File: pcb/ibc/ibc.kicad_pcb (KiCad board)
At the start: 2 copper layers, 87 x 80 mm, 72 parts, among them J1 MOLEX_0039291067, J2 CONN_01X03, J3 CONN_01X05, J4 MOLEX_0532610571, J5 U.FL, J6 U.FL, J7 U.FL, J8 U.FL, J9 MOLEX_0039291087, M1 LOGO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

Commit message: Finished v0.1 IBC ready for fab
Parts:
- added J10: GROUND, azonenberg_pcb:TESTPOINT_SMT_KEYSTONE_5016, F.Cu at (35.3, 52.7)
- added J11: GROUND, azonenberg_pcb:TESTPOINT_SMT_KEYSTONE_5016, F.Cu at (96.2, 78.5)
- moved C6 52.8 mm to (78.6, 79.7), turned to 180 degrees
- moved C4 52.5 mm to (78.0, 76.6), turned to 180 degrees
- moved C5 47.9 mm to (85.9, 86.0), turned to 180 degrees
- moved C9 46.7 mm to (86.6, 83.3)
- moved C8 40.8 mm to (86.7, 81.3)
- moved R9 38.3 mm to (99.4, 96.7), turned to 180 degrees
- moved R5 35.7 mm to (83.8, 85.5), turned to -90 degrees
- moved C3 33.6 mm to (92.2, 85.0), turned to -90 degrees
- moved FB2 29.5 mm to (91.5, 83.5)
- moved R23 1.16 mm to (95.8, 59.5), turned to -90 degrees
- moved R19 1.00 mm to (75.2, 82.8)
- moved R6 1.00 mm to (75.2, 81.2)
- moved R1 0.50 mm to (99.4, 69.5)
- moved R13 0.50 mm to (74.5, 59.5)
- moved R2 0.50 mm to (99.4, 71.5)
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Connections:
- U1 pad 10: /12V0_VSENSE -> /12V0_OUT_EN
- U1 pad 11: /12V0_OK -> /TEMP_ALERT
- U1 pad 12: unconnected-(U1-Pad12) -> /12V0_OK
- U1 pad 13: /LOAD_PGOOD -> /12V_SHUNT_VOUT
- U1 pad 14: /12V0_OUT_EN -> /12V0_REMOTE_VSENSE
- U1 pad 15: /12V0_REMOTE_VSENSE -> /12V0_VSENSE
- U1 pad 6: /TEMP_ALERT -> unconnected-(U1-Pad6)
- U1 pad 7: /12V_SHUNT_VOUT -> /48V_SHUNT_VOUT
- U1 pad 8: /48V_SHUNT_VOUT -> /48V0_VSENSE
- U1 pad 9: /48V0_VSENSE -> /LOAD_PGOOD
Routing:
- net /GND: track 0.00 -> 478.2 mm, vias 0 -> 151
- net /3V3_SB: track 0.00 -> 224.4 mm, vias 0 -> 9
- net /12V0_OUT_EN: track 0.00 -> 124.8 mm, vias 0 -> 3
- net /LOAD_PGOOD: track 0.00 -> 119.9 mm, vias 0 -> 2
- net /I2C_SDA: track 0.00 -> 82.6 mm, vias 0 -> 4
- net /I2C_SCL: track 0.00 -> 81.4 mm, vias 0 -> 2
- net /12V0_VSENSE: track 0.00 -> 77.7 mm
- net /12V_SHUNT_VOUT: track 0.00 -> 56.9 mm, vias 0 -> 2
- net /TEMP_ALERT: track 0.00 -> 54.6 mm, vias 0 -> 2
- net /12V0: track 0.00 -> 51.2 mm
- net /GND_RAW: track 0.00 -> 48.7 mm
- net /12V0_SENSE: track 0.00 -> 40.0 mm, vias 0 -> 2
- net /12V0_OK: track 0.00 -> 35.8 mm, vias 0 -> 2
- net /12V0_SWIN: track 0.00 -> 35.1 mm, vias 0 -> 6
- net /48V_SHIN: track 0.00 -> 31.7 mm
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- added copper zone on F.Cu, net /12V0
- added copper zone on F.Cu, net /12V0_RAW
- added copper zone on F.Cu, net /12V0_SHIN
- added copper zone on B.Cu, net /12V0_SWIN
- added copper zone on F.Cu, net /12V0_SWIN
- added copper zone on B.Cu, net /3V3_SB
- added copper zone on F.Cu, net /3V3_SB
- added copper zone on F.Cu, net /48V_SHIN
- added copper zone on B.Cu, net /GND
- added copper zone on F.Cu, net /GND
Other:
- board text added: "48VDC -> 12VDC Non-Isolated 72W Intermediate Bus Converter A. Zonenberg / v0.1 / 2023-10-18 S/N:"
- board text removed: "48VDC -> 12VDC Non-Isolated 72W Intermediate Bus Converter A. Zonenberg / v0.1 2023-10-15"

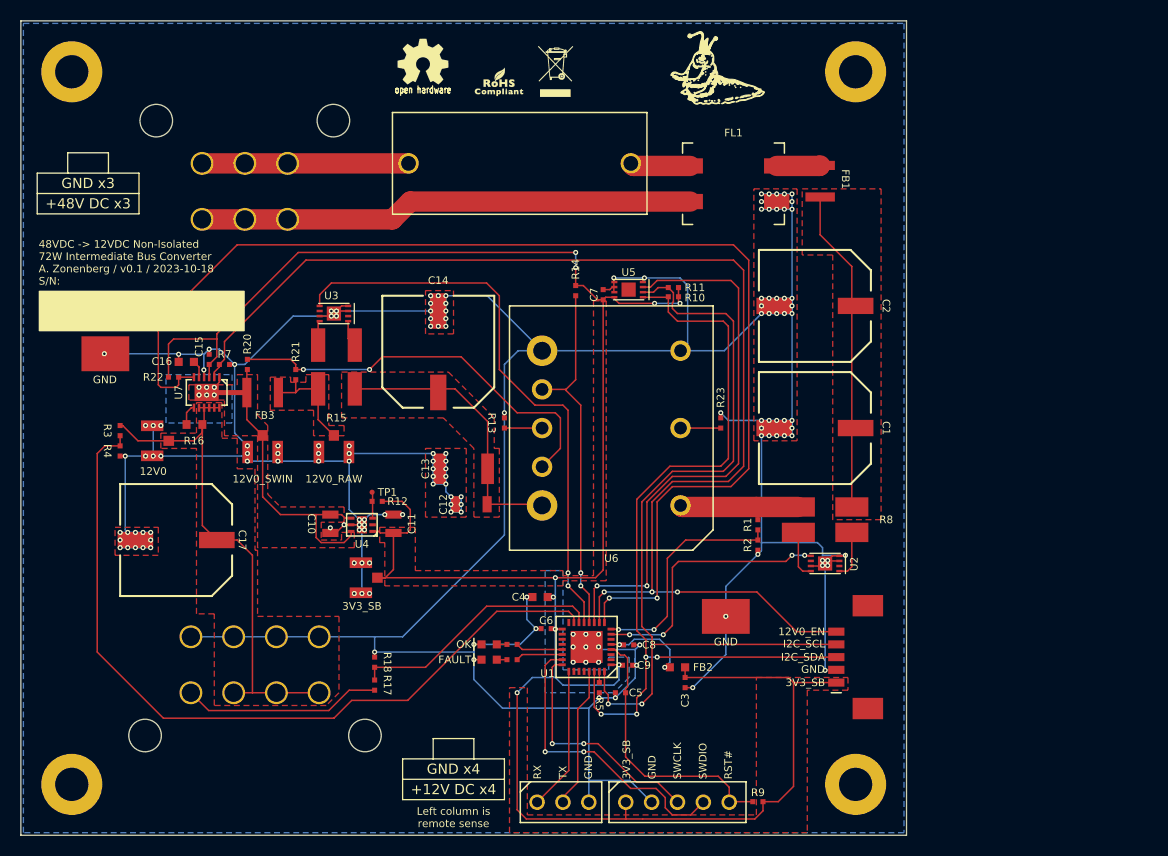
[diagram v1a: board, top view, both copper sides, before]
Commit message: Updated IBC board for v0.2 with antialiasing filter, plane fix, and 5V standby rail
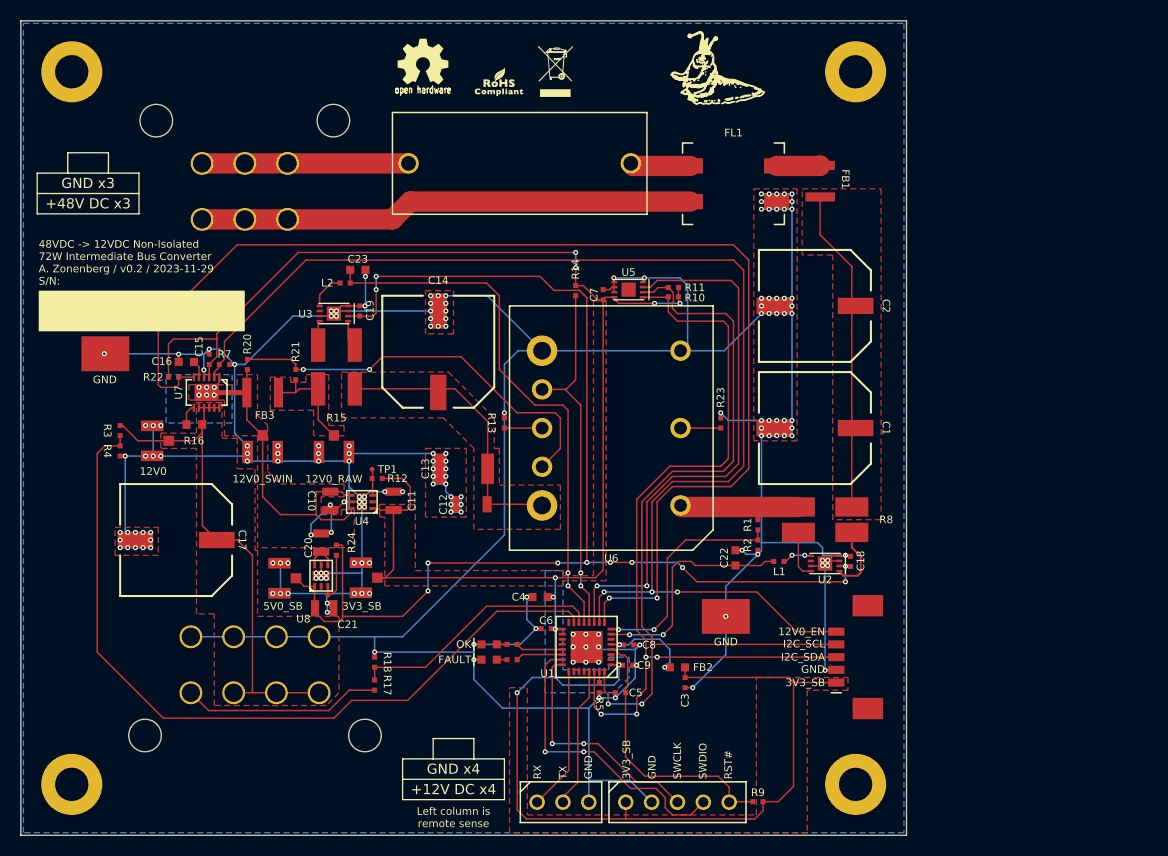
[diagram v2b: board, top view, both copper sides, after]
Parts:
- added C18: 0.47 uF, azonenberg_pcb:EIA_0402_CAP_NOSILK, F.Cu at (108.5, 73.1)
- added C19: 0.47 uF, azonenberg_pcb:EIA_0402_CAP_NOSILK, F.Cu at (60.3, 48.5)
- added C20: 2.2 uF, azonenberg_pcb:EIA_0805_CAP_NOSILK, F.Cu at (56.5, 71.2)
- added C21: 2.2 uF, azonenberg_pcb:EIA_0805_CAP_NOSILK, F.Cu at (56.8, 77.7)
- added C22: 4.7 uF, azonenberg_pcb:EIA_0603_CAP_NOSILK, F.Cu at (97.2, 72.8)
- added C23: 4.7 uF, azonenberg_pcb:EIA_0603_CAP_NOSILK, F.Cu at (60.1, 44.5)
- added J12: U.FL, azonenberg_pcb:CONN_U.FL_TE_1909763-1, F.Cu at (52.5, 74.8)
- added L1: 62 nH, azonenberg_pcb:EIA_0402_CAP_NOSILK, F.Cu at (101.5, 73.1)
- added L2: 62 nH, azonenberg_pcb:EIA_0402_CAP_NOSILK, F.Cu at (58.9, 45.8)
- added R24: 10K, azonenberg_pcb:EIA_0402_RES_NOSILK, F.Cu at (58.0, 72.0)
- added TP2: TESTPOINT, azonenberg_pcb:TESTPOINT_SMT_0.5MM, F.Cu at (57.1, 76.4)
- added U8: TPS7A2550DRVR, azonenberg_pcb:DFN_6_0.65MM_2x2MM, F.Cu at (56.5, 74.5)
- moved C10 2.25 mm to (57.4, 67.2)
- moved C11 2.25 mm to (63.6, 67.2)
- moved R12 2.25 mm to (62.0, 65.0)
- moved TP1 2.25 mm to (61.5, 64.0)
- moved U4 2.25 mm to (60.5, 67.2)
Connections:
- U1 pad 13: /12V_SHUNT_VOUT -> /12V_SHUNT_FILT
- U1 pad 7: /48V_SHUNT_VOUT -> /48V_SHUNT_FILT
- U2 pad 2: unconnected-(U2-Pad2) -> /5V0_SB
- U3 pad 2: unconnected-(U3-Pad2) -> /5V0_SB
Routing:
- net /5V0_SB: track 0.00 -> 126.5 mm, vias 0 -> 11
- net /12V_SHUNT_FILT: track 0.00 -> 53.6 mm, vias 0 -> 2
- net /12V_SHUNT_VOUT: track 56.9 -> 3.58 mm, vias 2 -> 0
- net /GND: track 478.2 -> 519.9 mm, vias 151 -> 170
- net /48V_SHUNT_VOUT: track 26.2 -> 2.72 mm, vias 4 -> 2
- net /48V_SHUNT_FILT: track 0.00 -> 22.6 mm, vias 0 -> 2
- net /5V0_SB_PGOOD: track 0.00 -> 5.17 mm
- net /12V0_SWIN: track 35.1 -> 38.2 mm
- net /3V3_SB: track 224.4 -> 226.7 mm
- net /48V_SHUNT_P: track 4.78 -> 6.75 mm
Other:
- board text added: "48VDC -> 12VDC Non-Isolated 72W Intermediate Bus Converter A. Zonenberg / v0.2 / 2023-11-29 S/N:"
- board text added: "5V0_SB"
- board text removed: "48VDC -> 12VDC Non-Isolated 72W Intermediate Bus Converter A. Zonenberg / v0.1 / 2023-10-18 S/N:"

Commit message: Respun again for v0.3, moving 48V shunt outside high dI/dT loop because I was derpy
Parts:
- moved C18 37.7 mm to (109.8, 35.4), turned to 180 degrees
- moved U2 35.7 mm to (110.0, 37.9), turned to 180 degrees
- moved L1 32.2 mm to (109.3, 41.9), turned to 90 degrees
- moved C22 31.6 mm to (108.6, 43.3), turned to 0 degrees
- moved R8 31.0 mm to (106.0, 38.0), turned to 180 degrees
- moved FB1 4.67 mm to (104.2, 31.2)
- moved C1 4.03 mm to (104.5, 64.0), turned to 180 degrees
- moved C2 4.03 mm to (104.5, 52.0)
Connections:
- C1 pad 1: /48V_SHIN -> /48V0
- C2 pad 1: /48V_SHIN -> /48V0
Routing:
- net /48V_SHUNT_FILT: track 22.6 -> 65.1 mm, vias 2 -> 4
- net /48V0: track 12.9 -> 48.0 mm
- net /48V_SHIN: track 31.7 -> 2.78 mm
- net /5V0_SB: track 126.5 -> 148.9 mm, vias 11 -> 8
- net /GND: track 519.9 -> 526.6 mm
- net /48V_CMC: track 4.29 -> 7.24 mm
- net /48V_SHUNT_VOUT: track 2.72 -> 1.87 mm
- net /A3V3: track 8.87 -> 8.23 mm
- added copper zone on F.Cu, net /48V0
- removed copper zone on F.Cu, net /48V_SHIN
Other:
- board text added: "48VDC -> 12VDC Non-Isolated 72W Intermediate Bus Converter A. Zonenberg / v0.3 / 2023-11-30 S/N:"
- board text removed: "48VDC -> 12VDC Non-Isolated 72W Intermediate Bus Converter A. Zonenberg / v0.2 / 2023-11-29 S/N:"
